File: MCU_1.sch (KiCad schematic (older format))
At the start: 18 parts, among them U2 STM32F051K6Ux

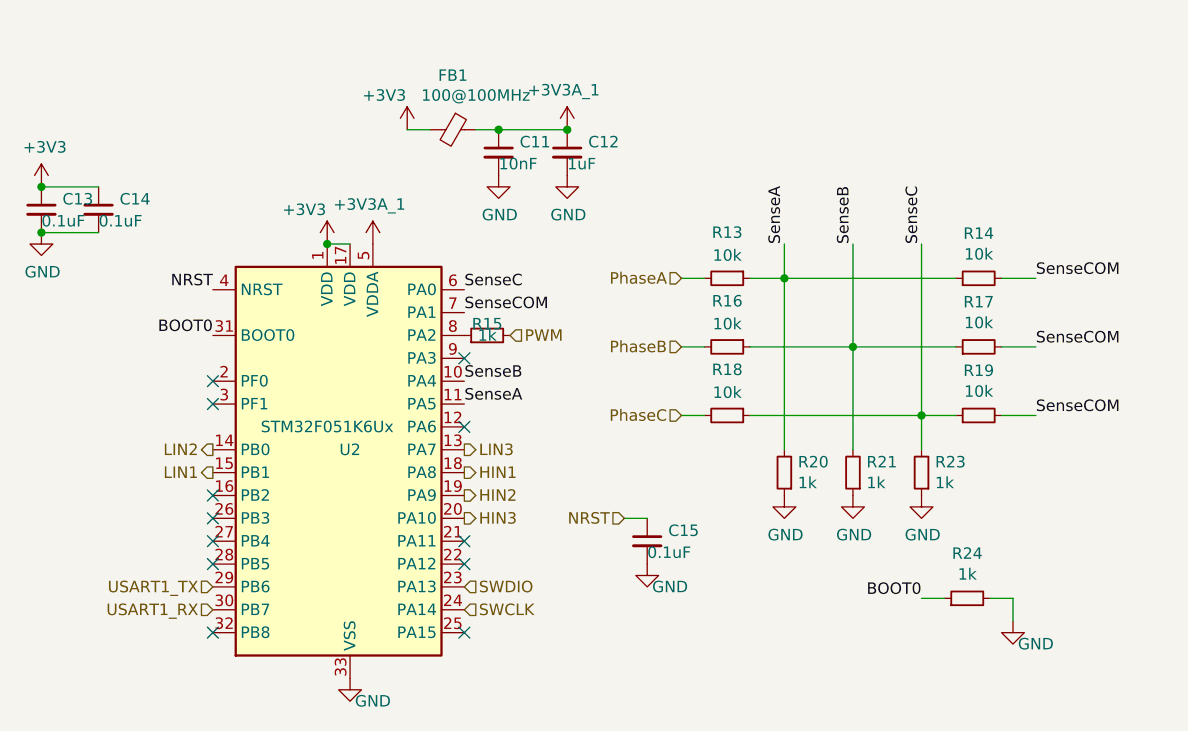
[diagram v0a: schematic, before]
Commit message: Lots of routing done to get rid of no-connects.  Down to 35 or so
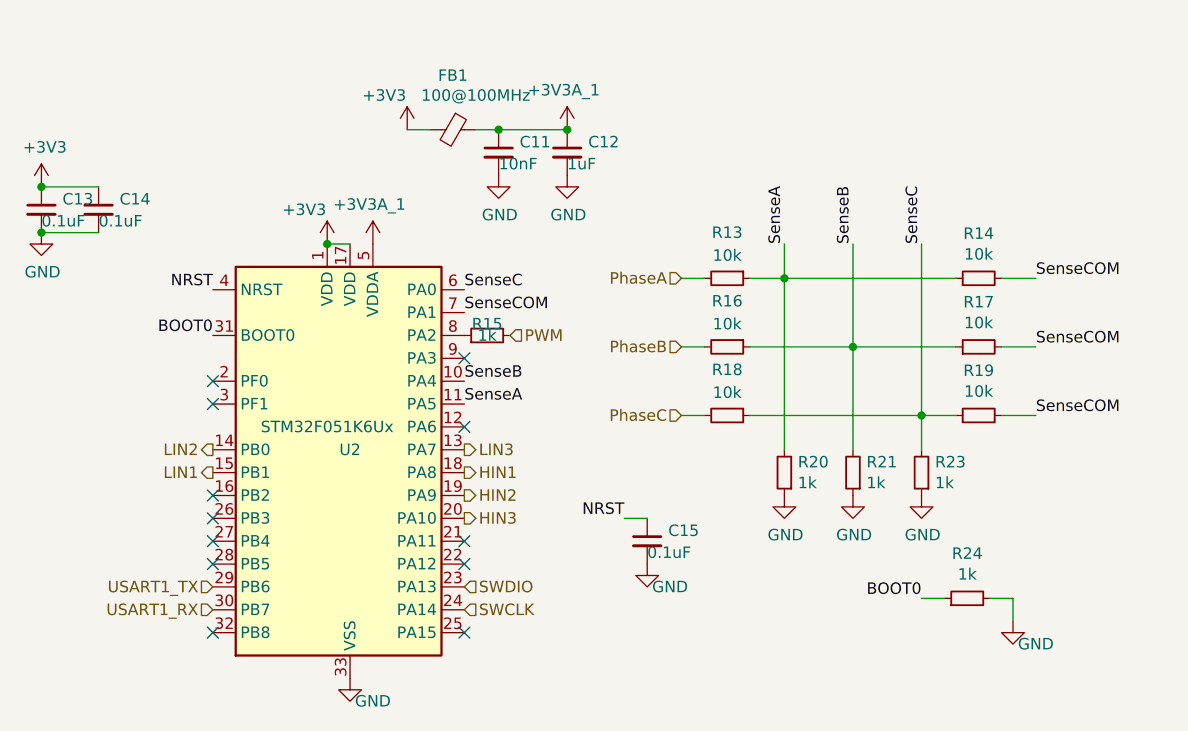
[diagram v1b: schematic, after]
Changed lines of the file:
@@
 $Descr A4 11693 8268
 encoding utf-8
-Sheet 9 11
+Sheet 8 11
 Title ""
 Date ""
@@
 Wire Wire Line
 	7050 2100 7050 2850
-Text HLabel 6350 3150 0    50   Input ~ 0
-NRST
 $Comp
 L power:+3V3 #PWR0110
@@
 $EndComp
 Connection ~ 6100 1450
+Text Label 6350 3150 2    50   ~ 0
+NRST
 $EndSCHEMATC

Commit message: Added stuff
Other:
- moved on the sheet: C11, C12, C15, FB1, R13, R14, R15, R16, R17, R18, R19, R20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
